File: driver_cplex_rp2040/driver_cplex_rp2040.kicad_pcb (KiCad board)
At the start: 6 copper layers, 40.2 x 40.2 mm, 391 parts, among them J1 Conn_01x05, J2 Conn_01x05, J5 USB_C_Receptacle_USB2.0, U2 AP2112K-3.3, U5 RP2040, U6 W25Q128JVS

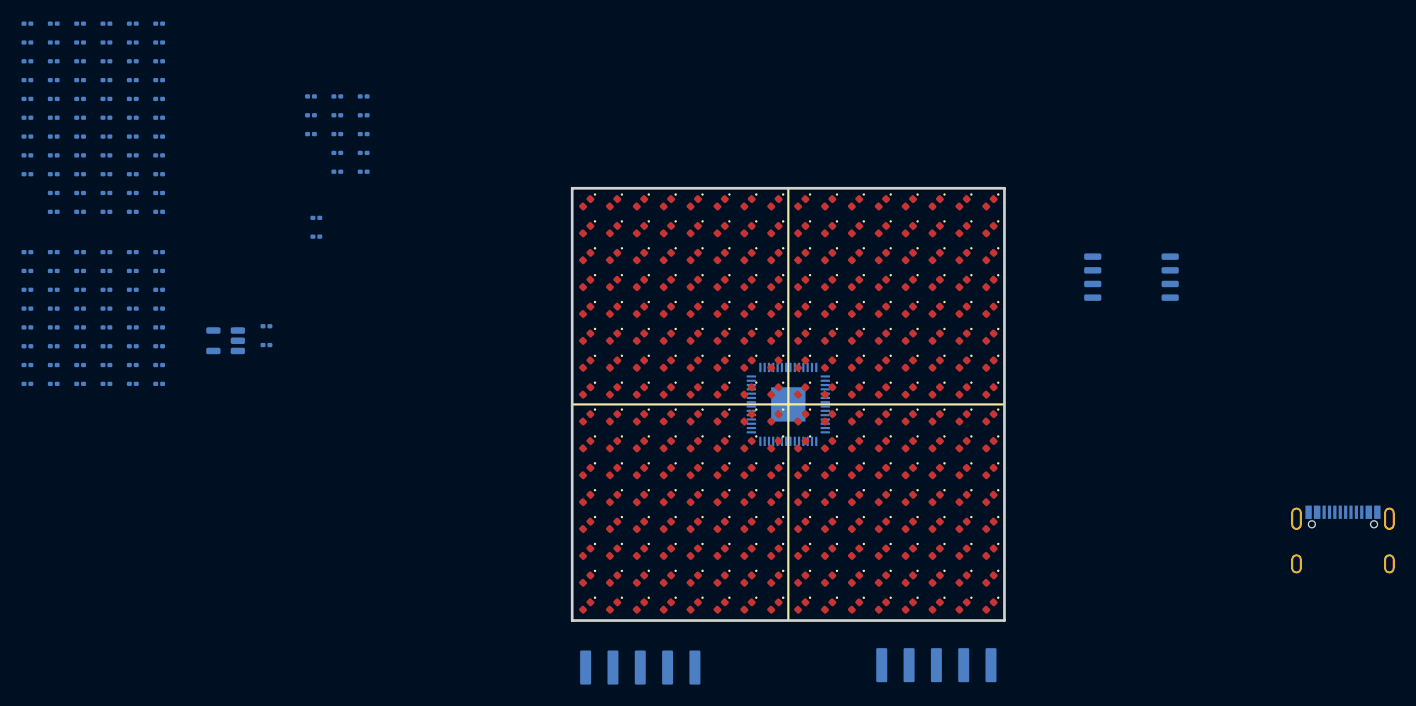
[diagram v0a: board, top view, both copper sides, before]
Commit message: Worked on footprint assignment for rp2040 single panel cplex design.
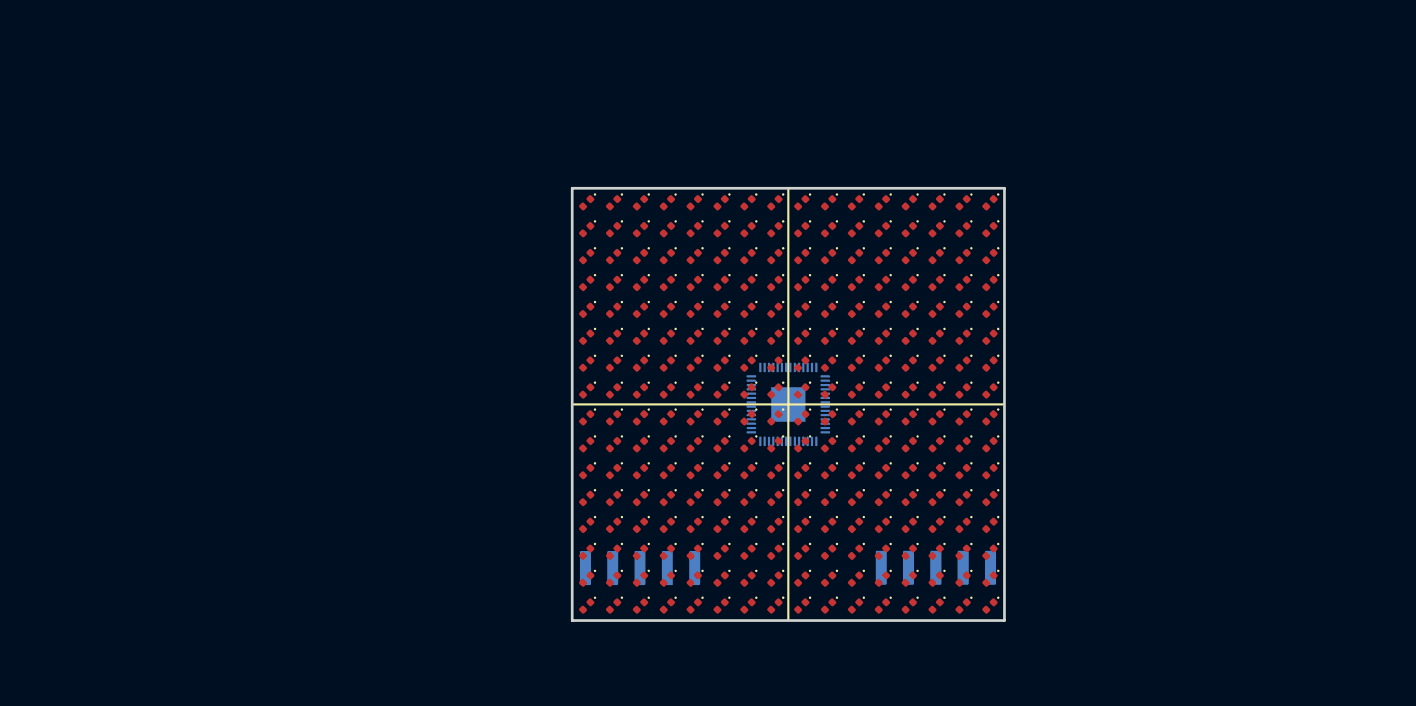
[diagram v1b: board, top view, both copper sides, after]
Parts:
- removed C1, C2: 20pF, panel_custom:C_0201_0603Metric
- removed C10, C11, C12, C13, C3, C4, C48, C49, C6, C7: 0.1uF, panel_custom:C_0201_0603Metric
- removed C17, C18, C19, C20, C21, C22, C23, C24, C25, C26, C27, C28, C29, C30, C31, C32: 200pF, panel_custom:C_0201_0603Metric
- removed C38, C47: 22uF, panel_custom:C_0201_0603Metric
- removed C5, C8, C9: 1uF, panel_custom:C_0201_0603Metric
- removed J5: USB_C_Receptacle_USB2.0, Connector_USB:USB_C_Receptacle_G-Switch_GT-USB-7010ASV
- removed R1, R17, R18, R19, R2, R20, R3, R4, R70, R71, R72, R73, R86, R87, R88, R89: 2k, panel_custom:R_0201_0603Metric
- removed R10, R101, R12, R14, R16, R26, R28, R30, R32, R79, R81, R83, R85, R95, R97, R99: 10k, panel_custom:R_0201_0603Metric
- removed R100, R11, R13, R15, R21, R22, R23, R24, R25, R27, R29, R31, R5, R6, R7, R74, R75, R76, R77, R78, R8, R80, R82, R84, R9, R90, R91, R92, R93, R94, R96, R98: 4.5k, panel_custom:R_0201_0603Metric
- removed R33, R34, R35, R36, R41, R42, R43, R44, R49, R50, R51, R52, R57, R58, R59, R60: 1k, panel_custom:R_0201_0603Metric
- removed R37, R38, R39, R40, R45, R46, R47, R48, R53, R54, R55, R56, R61, R62, R63, R64: 100, panel_custom:R_0201_0603Metric
- removed U2: AP2112K-3.3, Package_TO_SOT_SMD:SOT-23-5
- removed U6: W25Q128JVS, Package_SO:SOIC-8_5.23x5.23mm_P1.27mm
- moved J1 9.25 mm to (56.2, 85.2)
- moved J2 9.06 mm to (83.7, 85.2)

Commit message: Worked on layout.
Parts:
- added C1: 22uF, panel_custom:C_0402_1005Metric, B.Cu at (70.5, 51.2)
- added C10: 1uF, panel_custom:C_0201_0603Metric, F.Cu at (-4.35, 63.1)
- added C11: 0.1uF, panel_custom:C_0201_0603Metric, F.Cu at (-4.35, 64.8)
- added C12: 0.1uF, panel_custom:C_0201_0603Metric, F.Cu at (-4.35, 66.6)
- added C13: 0.1uF, panel_custom:C_0201_0603Metric, F.Cu at (-4.35, 68.3)
- added C14: 0.1uF, panel_custom:C_0201_0603Metric, F.Cu at (-4.35, 70.1)
- added C15: 0.1uF, panel_custom:C_0201_0603Metric, F.Cu at (-4.35, 71.8)
- added C2: 22uF, panel_custom:C_0402_1005Metric, B.Cu at (67.8, 53.8)
- added C3: 0.1uF, panel_custom:C_0201_0603Metric, F.Cu at (-6.80, 63.1)
- added C4: 20pF, panel_custom:C_0201_0603Metric, F.Cu at (-6.80, 64.8)
- added C5: 20pF, panel_custom:C_0201_0603Metric, F.Cu at (-6.80, 66.6)
- added C6: 1uF, panel_custom:C_0201_0603Metric, F.Cu at (-6.80, 68.3)
- added C7: 0.1uF, panel_custom:C_0201_0603Metric, F.Cu at (-6.80, 70.1)
- added C8: 0.1uF, panel_custom:C_0201_0603Metric, F.Cu at (-6.80, 71.8)
- added C9: 1uF, panel_custom:C_0201_0603Metric, F.Cu at (-6.80, 73.6)
- added J3: Conn_01x05, panel_custom:ConnRcpt_1x5_SMH-105-02-X-S, B.Cu at (82.7, 53.9)
- added J4: Conn_01x05, panel_custom:ConnRcpt_1x5_SMH-105-02-X-S, B.Cu at (57.3, 53.9)
- added J5: Conn_01x04, panel_custom:JST_SH_SM04B-SRSS-TB_1x04-1MP_P1.00mm_Horizontal, B.Cu at (70.0, 87.3)
- added Q1: 1xPNP and 1xNPN, panel_custom:SOT-963, F.Cu at (17.5, 14.9)
- added Q10: 1xPNP and 1xNPN, panel_custom:SOT-963, F.Cu at (20.5, 42.1)
- added Q11: 1xPNP and 1xNPN, panel_custom:SOT-963, F.Cu at (20.5, 44.6)
- added Q12: 1xPNP and 1xNPN, panel_custom:SOT-963, F.Cu at (20.5, 47.2)
- added Q13: 1xPNP and 1xNPN, panel_custom:SOT-963, F.Cu at (20.5, 49.7)
- added Q14: 1xPNP and 1xNPN, panel_custom:SOT-963, F.Cu at (20.5, 52.3)
- added Q15: 1xPNP and 1xNPN, panel_custom:SOT-963, F.Cu at (23.1, 37.0)
- added Q16: 1xPNP and 1xNPN, panel_custom:SOT-963, F.Cu at (23.1, 39.5)
- added Q17: 1xPNP and 1xNPN, panel_custom:SOT-963, F.Cu at (23.1, 42.1)
- added Q18: 1xPNP and 1xNPN, panel_custom:SOT-963, F.Cu at (23.1, 44.6)
- added Q19: 1xPNP and 1xNPN, panel_custom:SOT-963, F.Cu at (23.1, 47.2)
- added Q2: 1xPNP and 1xNPN, panel_custom:SOT-963, F.Cu at (17.5, 16.4)
- added Q20: 1xPNP and 1xNPN, panel_custom:SOT-963, F.Cu at (23.1, 49.7)
- added Q21: 1xPNP and 1xNPN, panel_custom:SOT-963, F.Cu at (23.1, 52.3)
- added Q22: 1xPNP and 1xNPN, panel_custom:SOT-963, F.Cu at (25.8, 37.0)
- added Q23: 1xPNP and 1xNPN, panel_custom:SOT-963, F.Cu at (25.8, 39.5)
- added Q24: 1xPNP and 1xNPN, panel_custom:SOT-963, F.Cu at (25.8, 42.1)
- added Q25: 1xPNP and 1xNPN, panel_custom:SOT-963, F.Cu at (25.8, 44.6)
- added Q26: 1xPNP and 1xNPN, panel_custom:SOT-963, F.Cu at (25.8, 47.2)
- added Q27: 1xPNP and 1xNPN, panel_custom:SOT-963, F.Cu at (25.8, 49.7)
- added Q28: 1xPNP and 1xNPN, panel_custom:SOT-963, F.Cu at (25.8, 52.3)
- added Q29: 1xPNP and 1xNPN, panel_custom:SOT-963, F.Cu at (28.4, 37.0)
- added Q3: 1xPNP and 1xNPN, panel_custom:SOT-963, F.Cu at (26.0, 15.0)
- added Q30: 1xPNP and 1xNPN, panel_custom:SOT-963, F.Cu at (28.4, 39.5)
- added Q31: 1xPNP and 1xNPN, panel_custom:SOT-963, F.Cu at (28.4, 42.1)
- added Q32: 1xPNP and 1xNPN, panel_custom:SOT-963, F.Cu at (28.4, 44.6)
- added Q33: 1xPNP and 1xNPN, panel_custom:SOT-963, F.Cu at (28.4, 47.2)
- added Q34: 1xPNP and 1xNPN, panel_custom:SOT-963, F.Cu at (28.4, 49.7)
- added Q4: 1xPNP and 1xNPN, panel_custom:SOT-963, F.Cu at (26.0, 16.5)
- added Q5: 1xPNP and 1xNPN, panel_custom:SOT-963, F.Cu at (34.1, 15.1)
- added Q6: 1xPNP and 1xNPN, panel_custom:SOT-963, F.Cu at (34.1, 16.6)
- added Q7: 1xPNP and 1xNPN, panel_custom:SOT-963, F.Cu at (17.8, 52.3)
- added Q8: 1xPNP and 1xNPN, panel_custom:SOT-963, F.Cu at (20.5, 37.0)
- added Q9: 1xPNP and 1xNPN, panel_custom:SOT-963, F.Cu at (20.5, 39.5)
- added R1: 27.4, panel_custom:R_0201_0603Metric, F.Cu at (-4.35, 73.6)
- added R10: 330, panel_custom:R_0201_0603Metric, F.Cu at (19.1, 16.1)
- added R100: 1k, panel_custom:R_0201_0603Metric, F.Cu at (7.90, 54.1)
- added R101: 1k, panel_custom:R_0201_0603Metric, F.Cu at (7.90, 55.8)
- added R102: 10, panel_custom:R_0201_0603Metric, F.Cu at (7.90, 57.6)
- added R103: 15k, panel_custom:R_0201_0603Metric, F.Cu at (7.90, 59.3)
- added R104: 15k, panel_custom:R_0201_0603Metric, F.Cu at (10.4, 36.6)
- added R105: 10k, panel_custom:R_0201_0603Metric, F.Cu at (10.4, 38.3)
- added R106: 330, panel_custom:R_0201_0603Metric, F.Cu at (10.4, 40.1)
- added R107: 330, panel_custom:R_0201_0603Metric, F.Cu at (10.4, 41.8)
- added R108: 1k, panel_custom:R_0201_0603Metric, F.Cu at (10.4, 43.6)
- added R109: 1k, panel_custom:R_0201_0603Metric, F.Cu at (10.4, 45.3)
- added R11: 330, panel_custom:R_0201_0603Metric, F.Cu at (15.9, 15.3)
- added R110: 10, panel_custom:R_0201_0603Metric, F.Cu at (10.4, 47.1)
- added R111: 15k, panel_custom:R_0201_0603Metric, F.Cu at (10.4, 48.8)
- added R112: 15k, panel_custom:R_0201_0603Metric, F.Cu at (10.4, 50.6)
- added R113: 10k, panel_custom:R_0201_0603Metric, F.Cu at (10.4, 52.3)
- added R114: 330, panel_custom:R_0201_0603Metric, F.Cu at (10.4, 54.1)
- added R115: 330, panel_custom:R_0201_0603Metric, F.Cu at (10.4, 55.8)
- added R116: 1k, panel_custom:R_0201_0603Metric, F.Cu at (10.4, 57.6)
- added R117: 1k, panel_custom:R_0201_0603Metric, F.Cu at (10.4, 59.3)
- added R118: 10, panel_custom:R_0201_0603Metric, F.Cu at (12.8, 36.6)
- added R119: 15k, panel_custom:R_0201_0603Metric, F.Cu at (12.8, 38.3)
- added R12: 1k, panel_custom:R_0201_0603Metric, F.Cu at (19.1, 16.9)
- added R120: 15k, panel_custom:R_0201_0603Metric, F.Cu at (12.8, 40.1)
- added R121: 10k, panel_custom:R_0201_0603Metric, F.Cu at (12.8, 41.8)
- added R122: 330, panel_custom:R_0201_0603Metric, F.Cu at (12.8, 43.6)
- added R123: 330, panel_custom:R_0201_0603Metric, F.Cu at (12.8, 45.3)
- added R124: 1k, panel_custom:R_0201_0603Metric, F.Cu at (12.8, 47.1)
- added R125: 1k, panel_custom:R_0201_0603Metric, F.Cu at (12.8, 48.8)
- added R126: 10, panel_custom:R_0201_0603Metric, F.Cu at (12.8, 50.6)
- added R127: 15k, panel_custom:R_0201_0603Metric, F.Cu at (12.8, 52.3)
- added R128: 15k, panel_custom:R_0201_0603Metric, F.Cu at (12.8, 54.1)
- added R129: 10k, panel_custom:R_0201_0603Metric, F.Cu at (12.8, 55.8)
- added R13: 1k, panel_custom:R_0201_0603Metric, F.Cu at (15.9, 14.5)
- added R130: 330, panel_custom:R_0201_0603Metric, F.Cu at (12.8, 57.6)
- added R131: 330, panel_custom:R_0201_0603Metric, F.Cu at (12.8, 59.3)
- added R132: 1k, panel_custom:R_0201_0603Metric, F.Cu at (15.3, 36.6)
- added R133: 1k, panel_custom:R_0201_0603Metric, F.Cu at (15.3, 38.3)
- added R134: 10, panel_custom:R_0201_0603Metric, F.Cu at (15.3, 40.1)
- added R135: 15k, panel_custom:R_0201_0603Metric, F.Cu at (15.3, 41.8)
- added R136: 15k, panel_custom:R_0201_0603Metric, F.Cu at (15.3, 43.6)
- added R137: 10k, panel_custom:R_0201_0603Metric, F.Cu at (15.3, 45.3)
- added R138: 330, panel_custom:R_0201_0603Metric, F.Cu at (15.3, 47.1)
- added R139: 330, panel_custom:R_0201_0603Metric, F.Cu at (15.3, 48.8)
- added R14: 10, panel_custom:R_0201_0603Metric, F.Cu at (27.6, 15.4)
- added R140: 1k, panel_custom:R_0201_0603Metric, F.Cu at (15.3, 50.6)
- added R141: 1k, panel_custom:R_0201_0603Metric, F.Cu at (15.3, 52.3)
- added R142: 270, panel_custom:R_0201_0603Metric, F.Cu at (19.9, 63.1)
- added R143: 270, panel_custom:R_0201_0603Metric, F.Cu at (19.9, 64.8)
- added R144: 270, panel_custom:R_0201_0603Metric, F.Cu at (19.9, 66.6)
- added R145: 270, panel_custom:R_0201_0603Metric, F.Cu at (19.9, 68.3)
- added R146: 270, panel_custom:R_0201_0603Metric, F.Cu at (19.9, 70.1)
- added R147: 270, panel_custom:R_0201_0603Metric, F.Cu at (19.9, 71.8)
- added R148: 270, panel_custom:R_0201_0603Metric, F.Cu at (22.4, 63.1)
- added R149: 270, panel_custom:R_0201_0603Metric, F.Cu at (22.4, 64.8)
- added R15: 15k, panel_custom:R_0201_0603Metric, F.Cu at (27.6, 14.6)
- added R150: 270, panel_custom:R_0201_0603Metric, F.Cu at (22.4, 66.6)
- added R151: 270, panel_custom:R_0201_0603Metric, F.Cu at (22.4, 68.3)
- added R152: 270, panel_custom:R_0201_0603Metric, F.Cu at (22.4, 70.1)
- added R153: 270, panel_custom:R_0201_0603Metric, F.Cu at (22.4, 71.8)
- added R154: 270, panel_custom:R_0201_0603Metric, F.Cu at (24.8, 63.1)
- added R155: 270, panel_custom:R_0201_0603Metric, F.Cu at (24.8, 64.8)
- added R156: 270, panel_custom:R_0201_0603Metric, F.Cu at (24.8, 66.6)
- added R157: 270, panel_custom:R_0201_0603Metric, F.Cu at (24.8, 68.3)
- added R158: 270, panel_custom:R_0201_0603Metric, F.Cu at (24.8, 70.1)
- added R16: 15k, panel_custom:R_0201_0603Metric, F.Cu at (24.5, 16.9)
- added R17: 10k, panel_custom:R_0201_0603Metric, F.Cu at (24.5, 16.1)
- added R18: 330, panel_custom:R_0201_0603Metric, F.Cu at (27.6, 16.1)
- added R19: 330, panel_custom:R_0201_0603Metric, F.Cu at (24.5, 15.4)
- added R2: 27.4, panel_custom:R_0201_0603Metric, F.Cu at (-1.90, 63.1)
- added R20: 1k, panel_custom:R_0201_0603Metric, F.Cu at (27.6, 16.9)
- added R21: 1k, panel_custom:R_0201_0603Metric, F.Cu at (24.5, 14.6)
- added R22: 10, panel_custom:R_0201_0603Metric, F.Cu at (35.7, 15.5)
- added R23: 15k, panel_custom:R_0201_0603Metric, F.Cu at (35.7, 14.7)
- added R24: 15k, panel_custom:R_0201_0603Metric, F.Cu at (32.5, 17.0)
- added R25: 10k, panel_custom:R_0201_0603Metric, F.Cu at (32.5, 16.2)
- added R26: 330, panel_custom:R_0201_0603Metric, F.Cu at (35.7, 16.2)
- added R27: 330, panel_custom:R_0201_0603Metric, F.Cu at (32.5, 15.5)
- added R28: 1k, panel_custom:R_0201_0603Metric, F.Cu at (35.7, 17.0)
- added R29: 1k, panel_custom:R_0201_0603Metric, F.Cu at (32.5, 14.7)
- added R3: 1k, panel_custom:R_0201_0603Metric, F.Cu at (-1.90, 64.8)
- added R30: 10, panel_custom:R_0201_0603Metric, F.Cu at (-4.35, 54.1)
- added R31: 15k, panel_custom:R_0201_0603Metric, F.Cu at (-4.35, 55.8)
- added R32: 15k, panel_custom:R_0201_0603Metric, F.Cu at (-4.35, 57.6)
- added R33: 10k, panel_custom:R_0201_0603Metric, F.Cu at (-4.35, 59.3)
- added R34: 330, panel_custom:R_0201_0603Metric, F.Cu at (-1.90, 36.6)
- added R35: 330, panel_custom:R_0201_0603Metric, F.Cu at (-1.90, 38.3)
- added R36: 1k, panel_custom:R_0201_0603Metric, F.Cu at (-1.90, 40.1)
- added R37: 1k, panel_custom:R_0201_0603Metric, F.Cu at (-1.90, 41.8)
- added R38: 10, panel_custom:R_0201_0603Metric, F.Cu at (-1.90, 43.6)
- added R39: 15k, panel_custom:R_0201_0603Metric, F.Cu at (-1.90, 45.3)
- added R4: 1k, panel_custom:R_0201_0603Metric, F.Cu at (-1.90, 66.6)
- added R40: 15k, panel_custom:R_0201_0603Metric, F.Cu at (-1.90, 47.1)
- added R41: 10k, panel_custom:R_0201_0603Metric, F.Cu at (-1.90, 48.8)
- added R42: 330, panel_custom:R_0201_0603Metric, F.Cu at (-1.90, 50.6)
- added R43: 330, panel_custom:R_0201_0603Metric, F.Cu at (-1.90, 52.3)
- added R44: 1k, panel_custom:R_0201_0603Metric, F.Cu at (-1.90, 54.1)
- added R45: 1k, panel_custom:R_0201_0603Metric, F.Cu at (-1.90, 55.8)
- added R46: 10, panel_custom:R_0201_0603Metric, F.Cu at (-1.90, 57.6)
- added R47: 15k, panel_custom:R_0201_0603Metric, F.Cu at (-1.90, 59.3)
- added R48: 15k, panel_custom:R_0201_0603Metric, F.Cu at (0.55, 36.6)
- added R49: 10k, panel_custom:R_0201_0603Metric, F.Cu at (0.55, 38.3)
- added R5: 10k, panel_custom:R_0201_0603Metric, F.Cu at (-1.90, 68.3)
- added R50: 330, panel_custom:R_0201_0603Metric, F.Cu at (0.55, 40.1)
- added R51: 330, panel_custom:R_0201_0603Metric, F.Cu at (0.55, 41.8)
- added R52: 1k, panel_custom:R_0201_0603Metric, F.Cu at (0.55, 43.6)
- added R53: 1k, panel_custom:R_0201_0603Metric, F.Cu at (0.55, 45.3)
- added R54: 10, panel_custom:R_0201_0603Metric, F.Cu at (0.55, 47.1)
- added R55: 15k, panel_custom:R_0201_0603Metric, F.Cu at (0.55, 48.8)
- added R56: 15k, panel_custom:R_0201_0603Metric, F.Cu at (0.55, 50.6)
- added R57: 10k, panel_custom:R_0201_0603Metric, F.Cu at (0.55, 52.3)
- added R58: 330, panel_custom:R_0201_0603Metric, F.Cu at (0.55, 54.1)
- added R59: 330, panel_custom:R_0201_0603Metric, F.Cu at (0.55, 55.8)
- added R6: 10, panel_custom:R_0201_0603Metric, F.Cu at (19.1, 15.3)
- added R60: 1k, panel_custom:R_0201_0603Metric, F.Cu at (0.55, 57.6)
- added R61: 1k, panel_custom:R_0201_0603Metric, F.Cu at (0.55, 59.3)
- added R62: 10, panel_custom:R_0201_0603Metric, F.Cu at (3.00, 36.6)
- added R63: 15k, panel_custom:R_0201_0603Metric, F.Cu at (3.00, 38.3)
- added R64: 15k, panel_custom:R_0201_0603Metric, F.Cu at (3.00, 40.1)
- added R65: 10k, panel_custom:R_0201_0603Metric, F.Cu at (3.00, 41.8)
- added R66: 330, panel_custom:R_0201_0603Metric, F.Cu at (3.00, 43.6)
- added R67: 330, panel_custom:R_0201_0603Metric, F.Cu at (3.00, 45.3)
- added R68: 1k, panel_custom:R_0201_0603Metric, F.Cu at (3.00, 47.1)
- added R69: 1k, panel_custom:R_0201_0603Metric, F.Cu at (3.00, 48.8)
- added R7: 15k, panel_custom:R_0201_0603Metric, F.Cu at (19.1, 14.5)
- added R70: 10, panel_custom:R_0201_0603Metric, F.Cu at (3.00, 50.6)
- added R71: 15k, panel_custom:R_0201_0603Metric, F.Cu at (3.00, 52.3)
- added R72: 15k, panel_custom:R_0201_0603Metric, F.Cu at (3.00, 54.1)
- added R73: 10k, panel_custom:R_0201_0603Metric, F.Cu at (3.00, 55.8)
- added R74: 330, panel_custom:R_0201_0603Metric, F.Cu at (3.00, 57.6)
- added R75: 330, panel_custom:R_0201_0603Metric, F.Cu at (3.00, 59.3)
- added R76: 1k, panel_custom:R_0201_0603Metric, F.Cu at (5.45, 36.6)
- added R77: 1k, panel_custom:R_0201_0603Metric, F.Cu at (5.45, 38.3)
- added R78: 10, panel_custom:R_0201_0603Metric, F.Cu at (5.45, 40.1)
- added R79: 15k, panel_custom:R_0201_0603Metric, F.Cu at (5.45, 41.8)
- added R8: 15k, panel_custom:R_0201_0603Metric, F.Cu at (15.9, 16.9)
- added R80: 15k, panel_custom:R_0201_0603Metric, F.Cu at (5.45, 43.6)
- added R81: 10k, panel_custom:R_0201_0603Metric, F.Cu at (5.45, 45.3)
- added R82: 330, panel_custom:R_0201_0603Metric, F.Cu at (5.45, 47.1)
- added R83: 330, panel_custom:R_0201_0603Metric, F.Cu at (5.45, 48.8)
- added R84: 1k, panel_custom:R_0201_0603Metric, F.Cu at (5.45, 50.6)
- added R85: 1k, panel_custom:R_0201_0603Metric, F.Cu at (5.45, 52.3)
- added R86: 10, panel_custom:R_0201_0603Metric, F.Cu at (5.45, 54.1)
- added R87: 15k, panel_custom:R_0201_0603Metric, F.Cu at (5.45, 55.8)
- added R88: 15k, panel_custom:R_0201_0603Metric, F.Cu at (5.45, 57.6)
- added R89: 10k, panel_custom:R_0201_0603Metric, F.Cu at (5.45, 59.3)
- added R9: 10k, panel_custom:R_0201_0603Metric, F.Cu at (15.9, 16.1)
- added R90: 330, panel_custom:R_0201_0603Metric, F.Cu at (7.90, 36.6)
- added R91: 330, panel_custom:R_0201_0603Metric, F.Cu at (7.90, 38.3)
- added R92: 1k, panel_custom:R_0201_0603Metric, F.Cu at (7.90, 40.1)
- added R93: 1k, panel_custom:R_0201_0603Metric, F.Cu at (7.90, 41.8)
- added R94: 10, panel_custom:R_0201_0603Metric, F.Cu at (7.90, 43.6)
- added R95: 15k, panel_custom:R_0201_0603Metric, F.Cu at (7.90, 45.3)
- added R96: 15k, panel_custom:R_0201_0603Metric, F.Cu at (7.90, 47.1)
- added R97: 10k, panel_custom:R_0201_0603Metric, F.Cu at (7.90, 48.8)
- added R98: 330, panel_custom:R_0201_0603Metric, F.Cu at (7.90, 50.6)
- added R99: 330, panel_custom:R_0201_0603Metric, F.Cu at (7.90, 52.3)
- added SW1: SW_Push, panel_custom:TS-1088-AR02016, B.Cu at (51.6, 70.0)
- added SW2: SW_Push, panel_custom:TS-1088-AR02016, B.Cu at (88.4, 70.0)
- added U1: AP2112K-3.3, Package_TO_SOT_SMD:SOT-23-5, B.Cu at (70.0, 53.8)
- added U3: W25Q16JVUXIQ_TR, panel_custom:flashmem_PSON50P300X200X60-9N, B.Cu at (80.8, 74.8)
- added Y1: 12MHz, panel_custom:Crystal_SMD_3225-4Pin_3.2x2.5mm, B.Cu at (59.6, 73.0)
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- renumbered U5 to U2
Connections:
- D1 pad 1: /panel_leds/ROW_00 -> /level_shifter/CP_5V_00
- D1 pad 2: Net-(D1-A) -> /level_shifter/CP_5V_01
- D10 pad 1: /panel_leds/ROW_09 -> /level_shifter/CP_5V_00
- D10 pad 2: Net-(D1-A) -> Net-(D10-A)
- D100 pad 1: /panel_leds/ROW_03 -> /level_shifter/CP_5V_06
- D101 pad 1: /panel_leds/ROW_04 -> /level_shifter/CP_5V_06
- D101 pad 2: Net-(D100-A) -> Net-(D101-A)
- D102 pad 1: /panel_leds/ROW_05 -> /level_shifter/CP_5V_06
- D102 pad 2: Net-(D100-A) -> Net-(D102-A)
- D103 pad 1: /panel_leds/ROW_06 -> /level_shifter/CP_5V_06
- D103 pad 2: Net-(D100-A) -> Net-(D103-A)
- D104 pad 1: /panel_leds/ROW_07 -> /level_shifter/CP_5V_06
- D104 pad 2: Net-(D100-A) -> Net-(D104-A)
- D105 pad 1: /panel_leds/ROW_08 -> /level_shifter/CP_5V_06
- D105 pad 2: Net-(D100-A) -> Net-(D105-A)
- D106 pad 1: /panel_leds/ROW_09 -> /level_shifter/CP_5V_06
- D106 pad 2: Net-(D100-A) -> Net-(D10-A)
- D107 pad 1: /panel_leds/ROW_10 -> /level_shifter/CP_5V_06
- D107 pad 2: Net-(D100-A) -> Net-(D107-A)
- D108 pad 1: /panel_leds/ROW_11 -> /level_shifter/CP_5V_06
- D108 pad 2: Net-(D100-A) -> Net-(D108-A)
- D109 pad 1: /panel_leds/ROW_12 -> /level_shifter/CP_5V_06
- D109 pad 2: Net-(D100-A) -> Net-(D109-A)
- D11 pad 1: /panel_leds/ROW_10 -> /level_shifter/CP_5V_00
- D11 pad 2: Net-(D1-A) -> Net-(D107-A)
- D110 pad 1: /panel_leds/ROW_13 -> /level_shifter/CP_5V_06
- D110 pad 2: Net-(D100-A) -> Net-(D110-A)
- D111 pad 1: /panel_leds/ROW_14 -> /level_shifter/CP_5V_06
- D111 pad 2: Net-(D100-A) -> Net-(D111-A)
- D112 pad 1: /panel_leds/ROW_15 -> /level_shifter/CP_5V_06
- D112 pad 2: Net-(D100-A) -> Net-(D112-A)
- D113 pad 1: /panel_leds/ROW_00 -> /level_shifter/CP_5V_07
- D114 pad 1: /panel_leds/ROW_01 -> /level_shifter/CP_5V_07
- D114 pad 2: Net-(D113-A) -> /level_shifter/CP_5V_01
- D115 pad 1: /panel_leds/ROW_02 -> /level_shifter/CP_5V_07
- D115 pad 2: Net-(D113-A) -> Net-(D115-A)
- D116 pad 1: /panel_leds/ROW_03 -> /level_shifter/CP_5V_07
- D116 pad 2: Net-(D113-A) -> Net-(D100-A)
- D117 pad 1: /panel_leds/ROW_04 -> /level_shifter/CP_5V_07
- D117 pad 2: Net-(D113-A) -> Net-(D101-A)
- D118 pad 1: /panel_leds/ROW_05 -> /level_shifter/CP_5V_07
- D118 pad 2: Net-(D113-A) -> Net-(D102-A)
- D119 pad 1: /panel_leds/ROW_06 -> /level_shifter/CP_5V_07
- D119 pad 2: Net-(D113-A) -> Net-(D119-A)
- D12 pad 1: /panel_leds/ROW_11 -> /level_shifter/CP_5V_00
- D12 pad 2: Net-(D1-A) -> Net-(D108-A)
- D120 pad 1: /panel_leds/ROW_07 -> /level_shifter/CP_5V_07
- D120 pad 2: Net-(D113-A) -> Net-(D104-A)
- D121 pad 1: /panel_leds/ROW_08 -> /level_shifter/CP_5V_07
- D121 pad 2: Net-(D113-A) -> Net-(D105-A)
- D122 pad 1: /panel_leds/ROW_09 -> /level_shifter/CP_5V_07
- D122 pad 2: Net-(D113-A) -> Net-(D10-A)
- D123 pad 1: /panel_leds/ROW_10 -> /level_shifter/CP_5V_07
- D123 pad 2: Net-(D113-A) -> Net-(D107-A)
- D124 pad 1: /panel_leds/ROW_11 -> /level_shifter/CP_5V_07
- D124 pad 2: Net-(D113-A) -> Net-(D108-A)
- D125 pad 1: /panel_leds/ROW_12 -> /level_shifter/CP_5V_07
- D125 pad 2: Net-(D113-A) -> Net-(D109-A)
- D126 pad 1: /panel_leds/ROW_13 -> /level_shifter/CP_5V_07
- D126 pad 2: Net-(D113-A) -> Net-(D110-A)
- D127 pad 1: /panel_leds/ROW_14 -> /level_shifter/CP_5V_07
- D127 pad 2: Net-(D113-A) -> Net-(D111-A)
- D128 pad 1: /panel_leds/ROW_15 -> /level_shifter/CP_5V_07
- D128 pad 2: Net-(D113-A) -> Net-(D112-A)
- D129 pad 1: /panel_leds/ROW_00 -> /level_shifter/CP_5V_08
- D129 pad 2: Net-(D129-A) -> Net-(D113-A)
- D13 pad 1: /panel_leds/ROW_12 -> /level_shifter/CP_5V_00
- D13 pad 2: Net-(D1-A) -> Net-(D109-A)
- D130 pad 1: /panel_leds/ROW_01 -> /level_shifter/CP_5V_08
- D130 pad 2: Net-(D129-A) -> /level_shifter/CP_5V_01
- D131 pad 1: /panel_leds/ROW_02 -> /level_shifter/CP_5V_08
- D131 pad 2: Net-(D129-A) -> Net-(D115-A)
- D132 pad 1: /panel_leds/ROW_03 -> /level_shifter/CP_5V_08
- D132 pad 2: Net-(D129-A) -> Net-(D100-A)
- D133 pad 1: /panel_leds/ROW_04 -> /level_shifter/CP_5V_08
- D133 pad 2: Net-(D129-A) -> Net-(D101-A)
- D134 pad 1: /panel_leds/ROW_05 -> /level_shifter/CP_5V_08
- D134 pad 2: Net-(D129-A) -> Net-(D102-A)
- D135 pad 1: /panel_leds/ROW_06 -> /level_shifter/CP_5V_08
- D135 pad 2: Net-(D129-A) -> Net-(D119-A)
- D136 pad 1: /panel_leds/ROW_07 -> /level_shifter/CP_5V_08
- D136 pad 2: Net-(D129-A) -> Net-(D103-A)
- D137 pad 1: /panel_leds/ROW_08 -> /level_shifter/CP_5V_08
- D137 pad 2: Net-(D129-A) -> Net-(D105-A)
- D138 pad 1: /panel_leds/ROW_09 -> /level_shifter/CP_5V_08
- D138 pad 2: Net-(D129-A) -> Net-(D10-A)
- D139 pad 1: /panel_leds/ROW_10 -> /level_shifter/CP_5V_08
- D139 pad 2: Net-(D129-A) -> Net-(D107-A)
- D14 pad 1: /panel_leds/ROW_13 -> /level_shifter/CP_5V_00
- D14 pad 2: Net-(D1-A) -> Net-(D110-A)
- D140 pad 1: /panel_leds/ROW_11 -> /level_shifter/CP_5V_08
- D140 pad 2: Net-(D129-A) -> Net-(D108-A)
- D141 pad 1: /panel_leds/ROW_12 -> /level_shifter/CP_5V_08
- D141 pad 2: Net-(D129-A) -> Net-(D109-A)
- D142 pad 1: /panel_leds/ROW_13 -> /level_shifter/CP_5V_08
- D142 pad 2: Net-(D129-A) -> Net-(D110-A)
- D143 pad 1: /panel_leds/ROW_14 -> /level_shifter/CP_5V_08
- D143 pad 2: Net-(D129-A) -> Net-(D111-A)
- D144 pad 1: /panel_leds/ROW_15 -> /level_shifter/CP_5V_08
- D144 pad 2: Net-(D129-A) -> Net-(D112-A)
- D145 pad 1: /panel_leds/ROW_00 -> /level_shifter/CP_5V_09
- D145 pad 2: Net-(D145-A) -> Net-(D113-A)
- D146 pad 1: /panel_leds/ROW_01 -> /level_shifter/CP_5V_09
- D146 pad 2: Net-(D145-A) -> /level_shifter/CP_5V_01
- D147 pad 1: /panel_leds/ROW_02 -> /level_shifter/CP_5V_09
- D147 pad 2: Net-(D145-A) -> Net-(D115-A)
- D148 pad 1: /panel_leds/ROW_03 -> /level_shifter/CP_5V_09
- D148 pad 2: Net-(D145-A) -> Net-(D100-A)
- D149 pad 1: /panel_leds/ROW_04 -> /level_shifter/CP_5V_09
- D149 pad 2: Net-(D145-A) -> Net-(D101-A)
- D15 pad 1: /panel_leds/ROW_14 -> /level_shifter/CP_5V_00
- D15 pad 2: Net-(D1-A) -> Net-(D111-A)
- D150 pad 1: /panel_leds/ROW_05 -> /level_shifter/CP_5V_09
- D150 pad 2: Net-(D145-A) -> Net-(D102-A)
- D151 pad 1: /panel_leds/ROW_06 -> /level_shifter/CP_5V_09
- D151 pad 2: Net-(D145-A) -> Net-(D119-A)
- D152 pad 1: /panel_leds/ROW_07 -> /level_shifter/CP_5V_09
- D152 pad 2: Net-(D145-A) -> Net-(D103-A)
- D153 pad 1: /panel_leds/ROW_08 -> /level_shifter/CP_5V_09
- D153 pad 2: Net-(D145-A) -> Net-(D104-A)
- D154 pad 1: /panel_leds/ROW_09 -> /level_shifter/CP_5V_09
- D154 pad 2: Net-(D145-A) -> Net-(D10-A)
- D155 pad 1: /panel_leds/ROW_10 -> /level_shifter/CP_5V_09
- D155 pad 2: Net-(D145-A) -> Net-(D107-A)
- D156 pad 1: /panel_leds/ROW_11 -> /level_shifter/CP_5V_09
- D156 pad 2: Net-(D145-A) -> Net-(D108-A)
- D157 pad 1: /panel_leds/ROW_12 -> /level_shifter/CP_5V_09
- D157 pad 2: Net-(D145-A) -> Net-(D109-A)
- D158 pad 1: /panel_leds/ROW_13 -> /level_shifter/CP_5V_09
- D158 pad 2: Net-(D145-A) -> Net-(D110-A)
- D159 pad 1: /panel_leds/ROW_14 -> /level_shifter/CP_5V_09
- D159 pad 2: Net-(D145-A) -> Net-(D111-A)
- D16 pad 1: /panel_leds/ROW_15 -> /level_shifter/CP_5V_00
- D16 pad 2: Net-(D1-A) -> Net-(D112-A)
- D160 pad 1: /panel_leds/ROW_15 -> /level_shifter/CP_5V_09
- D160 pad 2: Net-(D145-A) -> Net-(D112-A)
- D161 pad 1: /panel_leds/ROW_00 -> /level_shifter/CP_5V_10
- D161 pad 2: Net-(D161-A) -> Net-(D113-A)
- D162 pad 1: /panel_leds/ROW_01 -> /level_shifter/CP_5V_10
- D162 pad 2: Net-(D161-A) -> /level_shifter/CP_5V_01
- D163 pad 1: /panel_leds/ROW_02 -> /level_shifter/CP_5V_10
- D163 pad 2: Net-(D161-A) -> Net-(D115-A)
- D164 pad 1: /panel_leds/ROW_03 -> /level_shifter/CP_5V_10
- D164 pad 2: Net-(D161-A) -> Net-(D100-A)
- D165 pad 1: /panel_leds/ROW_04 -> /level_shifter/CP_5V_10
- D165 pad 2: Net-(D161-A) -> Net-(D101-A)
- D166 pad 1: /panel_leds/ROW_05 -> /level_shifter/CP_5V_10
- D166 pad 2: Net-(D161-A) -> Net-(D102-A)
- D167 pad 1: /panel_leds/ROW_06 -> /level_shifter/CP_5V_10
- D167 pad 2: Net-(D161-A) -> Net-(D119-A)
- D168 pad 1: /panel_leds/ROW_07 -> /level_shifter/CP_5V_10
- D168 pad 2: Net-(D161-A) -> Net-(D103-A)
- D169 pad 1: /panel_leds/ROW_08 -> /level_shifter/CP_5V_10
- D169 pad 2: Net-(D161-A) -> Net-(D104-A)
- D17 pad 1: /panel_leds/ROW_00 -> /level_shifter/CP_5V_01
- D17 pad 2: Net-(D17-A) -> Net-(D113-A)
- D170 pad 1: /panel_leds/ROW_09 -> /level_shifter/CP_5V_10
- D170 pad 2: Net-(D161-A) -> Net-(D105-A)
- D171 pad 1: /panel_leds/ROW_10 -> /level_shifter/CP_5V_10
- D171 pad 2: Net-(D161-A) -> Net-(D107-A)
- D172 pad 1: /panel_leds/ROW_11 -> /level_shifter/CP_5V_10
- D172 pad 2: Net-(D161-A) -> Net-(D108-A)
- D173 pad 1: /panel_leds/ROW_12 -> /level_shifter/CP_5V_10
- D173 pad 2: Net-(D161-A) -> Net-(D109-A)
- D174 pad 1: /panel_leds/ROW_13 -> /level_shifter/CP_5V_10
- D174 pad 2: Net-(D161-A) -> Net-(D110-A)
- D175 pad 1: /panel_leds/ROW_14 -> /level_shifter/CP_5V_10
- D175 pad 2: Net-(D161-A) -> Net-(D111-A)
- D176 pad 1: /panel_leds/ROW_15 -> /level_shifter/CP_5V_10
- D176 pad 2: Net-(D161-A) -> Net-(D112-A)
- D177 pad 1: /panel_leds/ROW_00 -> /level_shifter/CP_5V_11
- D177 pad 2: Net-(D177-A) -> Net-(D113-A)
- D178 pad 1: /panel_leds/ROW_01 -> /level_shifter/CP_5V_11
- D178 pad 2: Net-(D177-A) -> /level_shifter/CP_5V_01
- D179 pad 1: /panel_leds/ROW_02 -> /level_shifter/CP_5V_11
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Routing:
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
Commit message: Worked on layout.
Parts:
- Q3, Q4, R14, R15, R16, R17, R18, R19, R20, R21: moved to B.Cu
- moved R14 3.80 mm to (23.8, 15.2), turned to 0 degrees
- moved R15 3.80 mm to (23.8, 14.4), turned to 180 degrees
- moved R18 3.80 mm to (23.8, 16.0), turned to 0 degrees
- moved R20 3.80 mm to (23.8, 16.8), turned to 180 degrees
- moved R16 2.45 mm to (26.9, 16.8), turned to 180 degrees
- moved R17 2.45 mm to (26.9, 16.0), turned to 0 degrees
- moved R19 2.45 mm to (26.9, 15.2), turned to 0 degrees
- moved R21 2.45 mm to (26.9, 14.4), turned to 0 degrees
- moved Q4 0.69 mm to (25.3, 16.4), turned to 180 degrees
- moved Q3 0.69 mm to (25.3, 14.8), turned to 180 degrees
- moved SW1 0.64 mm to (51.7, 70.6)
- moved SW2 0.48 mm to (88.3, 70.5)

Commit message: minor mods to rp2040 cplex design.
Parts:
- moved R118 291.9 mm to (285.7, 140.1)
- moved R119 291.9 mm to (285.7, 141.9)
- moved R120 291.9 mm to (285.7, 143.6)
- moved R121 291.9 mm to (285.7, 145.4)
- moved R122 291.9 mm to (285.7, 147.1)
- moved R123 291.9 mm to (285.7, 148.9)
- moved R124 291.9 mm to (285.7, 150.6)
- moved R125 291.9 mm to (285.7, 152.4)
- moved Q29 268.0 mm to (274.9, 142.1)
- moved Q30 268.0 mm to (274.9, 144.6)
- moved R110 267.5 mm to (261.3, 139.8)
- moved R111 267.5 mm to (261.3, 141.6)
- moved R112 267.5 mm to (261.3, 143.3)
- moved R113 267.5 mm to (261.3, 145.1)
- moved R114 267.5 mm to (261.3, 146.8)
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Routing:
- net /level_shifter/CP_3V3_00: track 7.53 -> 0.00 mm
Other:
- board text added: "tri-state levelshifter"
- board text added: "tri-state levelshifter internal routing"

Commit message: Worked on cplex driver layout.
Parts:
- Q3, Q4, R14, R15, R16, R17, R18, R19, R20, R21: moved to F.Cu
- moved R61 131.6 mm to (81.2, 21.5), turned to 180 degrees
- moved R33 130.9 mm to (53.5, 22.9), turned to 180 degrees
- moved R47 130.7 mm to (75.0, 21.5)
- moved R45 130.6 mm to (62.5, 21.5), turned to 180 degrees
- moved R31 129.6 mm to (56.6, 21.3)
- moved Q7 129.3 mm to (55.1, 21.7)
- moved R32 128.4 mm to (53.5, 23.7)
- moved R46 128.1 mm to (75.0, 22.3), turned to 180 degrees
- moved R59 127.4 mm to (81.2, 22.3), turned to 180 degrees
- moved R60 127.2 mm to (84.3, 23.8)
- moved R30 127.1 mm to (56.6, 22.1), turned to 180 degrees
- moved R53 127.0 mm to (71.9, 21.5), turned to 180 degrees
- moved R44 126.8 mm to (65.7, 23.8)
- moved R43 126.3 mm to (62.5, 22.3), turned to 180 degrees
- moved R37 125.0 mm to (53.5, 21.3), turned to 180 degrees
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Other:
- board text removed: "tri-state levelshifter"
- board text removed: "tri-state levelshifter internal routing"

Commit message: Worked on rp2040 cplex panel layout.
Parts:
- moved R93 144.6 mm to (116.4, 21.4), turned to 180 degrees
- moved R85 143.8 mm to (108.2, 21.5), turned to 180 degrees
- moved Q21 140.0 mm to (117.9, 21.8)
- moved R83 139.9 mm to (108.2, 22.3), turned to 180 degrees
- moved R84 138.7 mm to (111.3, 23.8)
- moved R75 137.1 mm to (98.8, 22.2), turned to 180 degrees
- moved R82 136.3 mm to (111.3, 23.0), turned to 180 degrees
- moved R90 136.3 mm to (132.9, 16.6)
- moved R91 136.3 mm to (132.9, 18.4)
- moved R92 136.3 mm to (132.9, 20.1)
- moved R86 136.3 mm to (132.8, 24.1)
- moved R87 136.3 mm to (132.8, 25.9)
- moved R88 136.3 mm to (132.8, 27.6)
- moved R89 136.3 mm to (132.8, 29.4)
- moved R81 136.1 mm to (108.2, 23.0), turned to 180 degrees
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
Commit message: Worked on rp2040 cplex layout.
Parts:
- added C15: 0.1uF, panel_custom:C_0201_0603Metric, B.Cu at (72.8, 67.8)
- added C16: 0.1uF, panel_custom:C_0201_0603Metric, B.Cu at (75.0, 69.8)
- added C17: 0.1uF, panel_custom:C_0201_0603Metric, B.Cu at (75.0, 72.2)
- added C18: 0.1uF, panel_custom:C_0201_0603Metric, B.Cu at (64.8, 70.9)
- added C20: 0.1uF, panel_custom:C_0201_0603Metric, B.Cu at (75.0, 72.9)
- C10, C11, C12, C13, C14, C3, C4, C5, C6, C7, C8, C9, Q1, Q2, R1, R10, R11, R12, R13, R142, R2, R3, R4, R5, R6, R7, R8, R9: moved to B.Cu
- C19: renamed from C15; moved to B.Cu
- moved R130 199.2 mm to (165.7, 23.1), turned to 180 degrees
- moved Q32 199.1 mm to (164.1, 23.5)
- moved R131 199.0 mm to (162.6, 22.3), turned to 180 degrees
- moved Q31 198.4 mm to (164.1, 21.9)
- moved R127 196.5 mm to (165.7, 21.5)
- moved R129 195.8 mm to (162.6, 23.1), turned to 180 degrees
- moved R126 194.7 mm to (165.7, 22.3), turned to 180 degrees
- moved R128 194.0 mm to (162.6, 23.9)
- moved Q34 191.7 mm to (173.1, 23.5)
- moved R133 191.5 mm to (162.6, 21.5), turned to 180 degrees
- moved Q33 191.0 mm to (173.1, 21.9)
- moved R132 190.7 mm to (165.7, 23.9)
- moved R141 190.5 mm to (171.5, 21.5), turned to 180 degrees
- moved R140 189.2 mm to (174.7, 23.9)
- moved R138 187.1 mm to (174.7, 23.1), turned to 180 degrees
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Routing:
- net /level_shifter/CP_5V_00: track 2.93 -> 4.39 mm

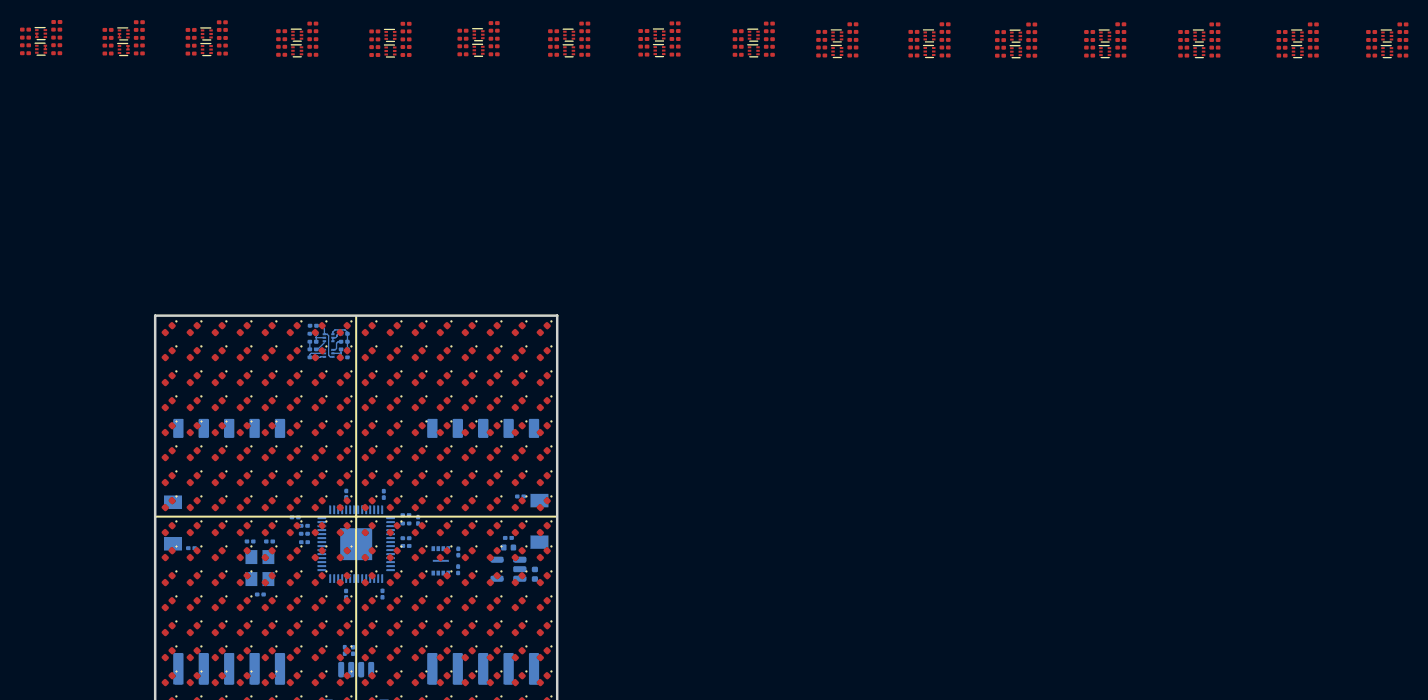
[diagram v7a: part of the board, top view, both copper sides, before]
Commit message: Worked on layout for rp2040 cplex'd panel.
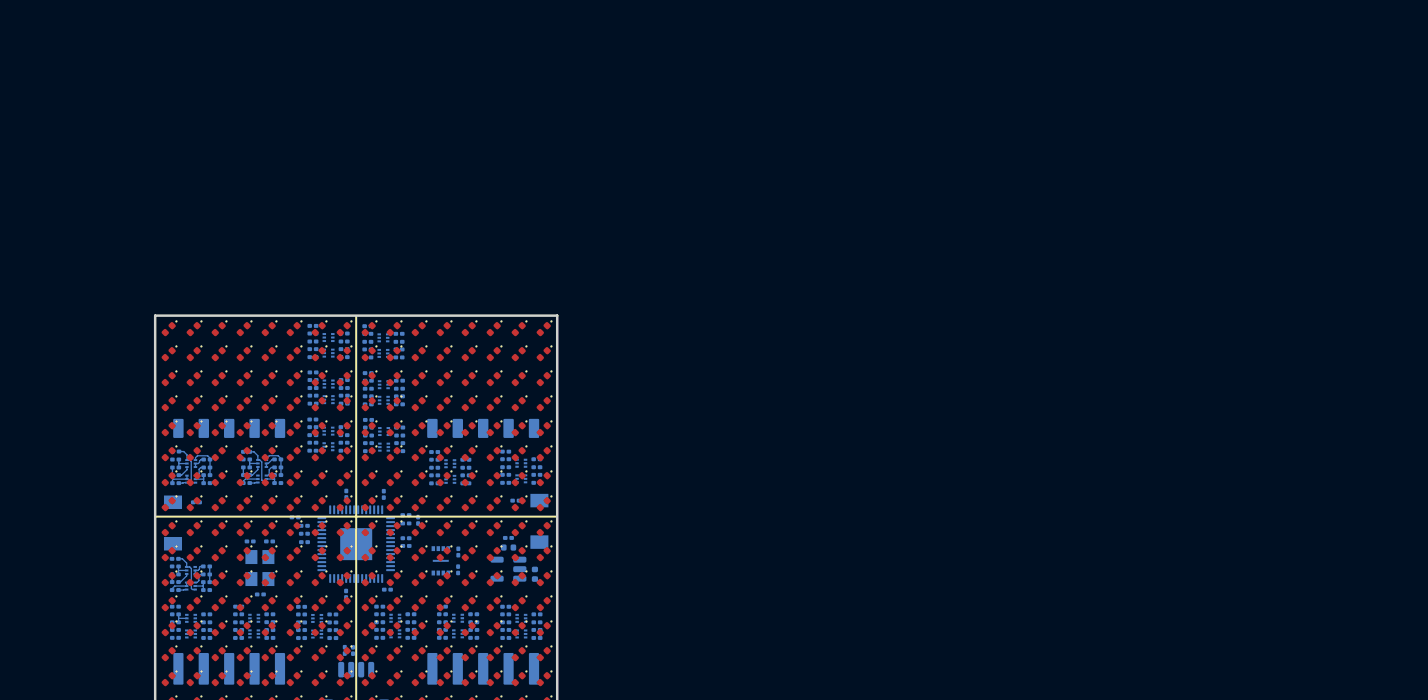
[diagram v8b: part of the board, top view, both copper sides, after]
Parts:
- Q10, Q11, Q12, Q13, Q14, Q15, Q16, Q17, Q18, Q19, Q20, Q21, Q22, Q23, Q24, Q25, Q26, Q27, Q28, Q29, Q3, Q30, Q31, Q32, Q33, Q34, Q4, Q5, Q6, Q7, Q8, Q9, R100, R101, R102, R103, R104, R105, R106, R107, R108, R109, R110, R111, R112, R113, R114, R115, R116, R117, R118, R119, R120, R121, R122, R123, R124, R125, R126, R127, R128, R129, R130, R131, R132, R133, R134, R135, R136, R137, R138, R139, R14, R140, R141, R143, R144, R145, R146, R147, R148, R149, R15, R150, R151, R152, R153, R154, R155, R156, R157, R158, R16, R17, R18, R19, R20, R21, R22, R23, R24, R25, R26, R27, R28, R29, R30, R31, R32, R33, R34, R35, R36, R37, R38, R39, R40, R41, R42, R43, R44, R45, R46, R47, R48, R49, R50, R51, R52, R53, R54, R55, R56, R57, R58, R59, R60, R61, R62, R63, R64, R65, R66, R67, R68, R69, R70, R71, R72, R73, R74, R75, R76, R77, R78, R79, R80, R81, R82, R83, R84, R85, R86, R87, R88, R89, R90, R91, R92, R93, R94, R95, R96, R97, R98, R99: moved to B.Cu
- moved R135 107.0 mm to (84.9, 79.8), turned to 180 degrees
- moved R158 107.0 mm to (84.9, 79.0), turned to 180 degrees
- moved R134 106.9 mm to (85.0, 80.6), turned to 0 degrees
- moved R138 106.9 mm to (85.0, 81.3), turned to 0 degrees
- moved R140 106.9 mm to (85.0, 82.1), turned to 180 degrees
- moved R127 104.7 mm to (78.6, 79.8), turned to 180 degrees
- moved R132 104.7 mm to (78.6, 82.1), turned to 180 degrees
- moved R126 104.7 mm to (78.6, 80.6), turned to 0 degrees
- moved R130 104.7 mm to (78.6, 81.3), turned to 0 degrees
- moved R157 104.7 mm to (78.6, 79.0), turned to 180 degrees
- moved Q33 104.3 mm to (86.5, 80.2), turned to 180 degrees
- moved Q34 104.3 mm to (86.5, 81.7), turned to 180 degrees
- moved Q31 102.2 mm to (80.2, 80.2), turned to 180 degrees
- moved Q32 102.2 mm to (80.2, 81.7), turned to 180 degrees
- moved R136 101.8 mm to (88.1, 82.1), turned to 180 degrees
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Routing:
- net GND: track 3.56 -> 8.61 mm
- net /level_shifter/CP_5V_01: track 0.00 -> 4.35 mm
- net /level_shifter/CP_5V_04: track 0.00 -> 4.24 mm
- net Net-(Q10-Pad5): track 0.00 -> 1.73 mm
- net Net-(Q4-Pad5): track 0.35 -> 2.05 mm
- net +5V: track 0.84 -> 2.51 mm
- net Net-(Q10-Pad2): track 0.00 -> 1.63 mm
- net Net-(Q9-Pad5): track 0.00 -> 1.62 mm
- net Net-(Q5-Pad5): track 0.00 -> 1.62 mm
- net Net-(Q3-Pad5): track 0.00 -> 1.61 mm
- net Net-(Q4-Pad2): track 0.00 -> 1.61 mm
- net +3.3V: track 0.76 -> 2.28 mm
- net Net-(Q10-Pad1): track 0.00 -> 1.43 mm
- net Net-(Q4-Pad1): track 0.00 -> 1.41 mm
- net Net-(Q9-Pad2): track 0.00 -> 1.33 mm
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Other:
- board text removed: "BOT"
- board text removed: "TOP"
